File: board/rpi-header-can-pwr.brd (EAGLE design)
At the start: 87 x 56.5 mm, 66 parts, among them J1 U.FL, U1 MCP2515, U2 ADS1015, U3 BME280, U4 RFM69HCW, X2 RASPI_BOARD_B+#_E3

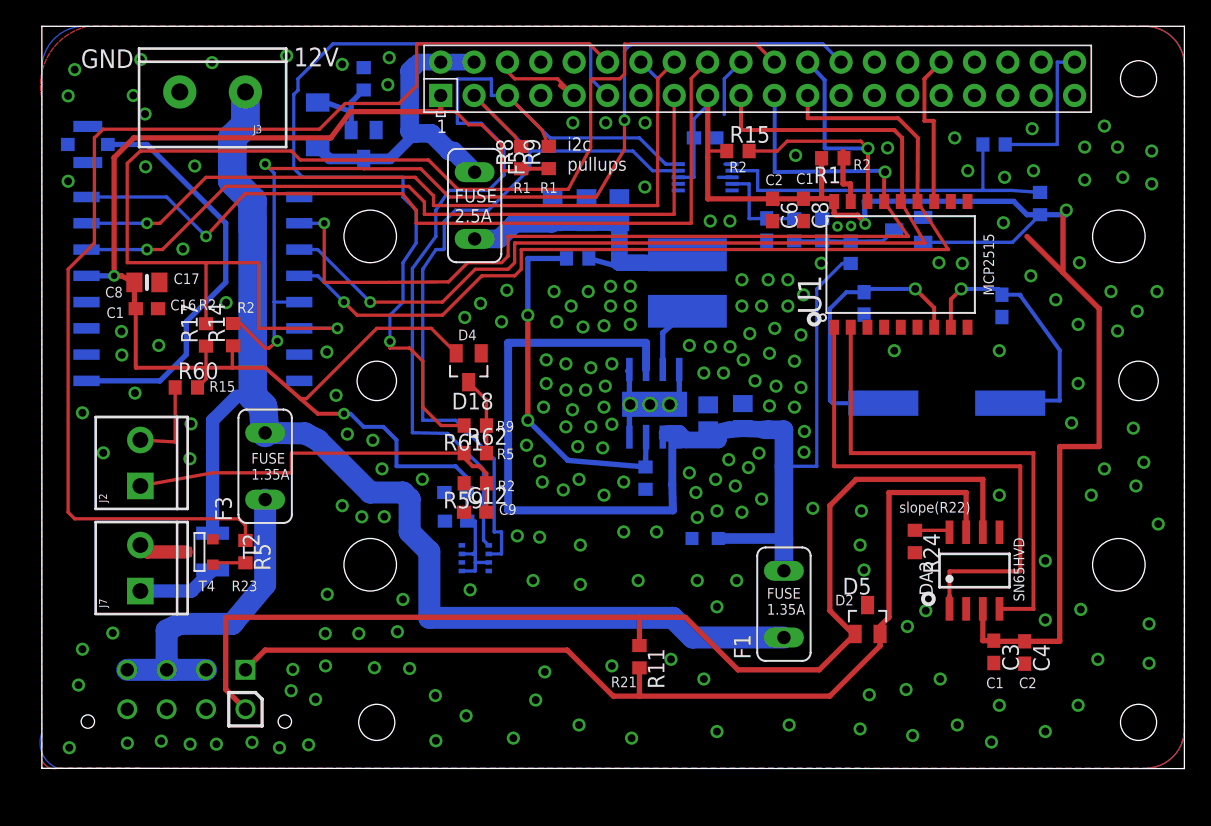
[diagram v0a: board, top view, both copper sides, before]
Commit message: add in219
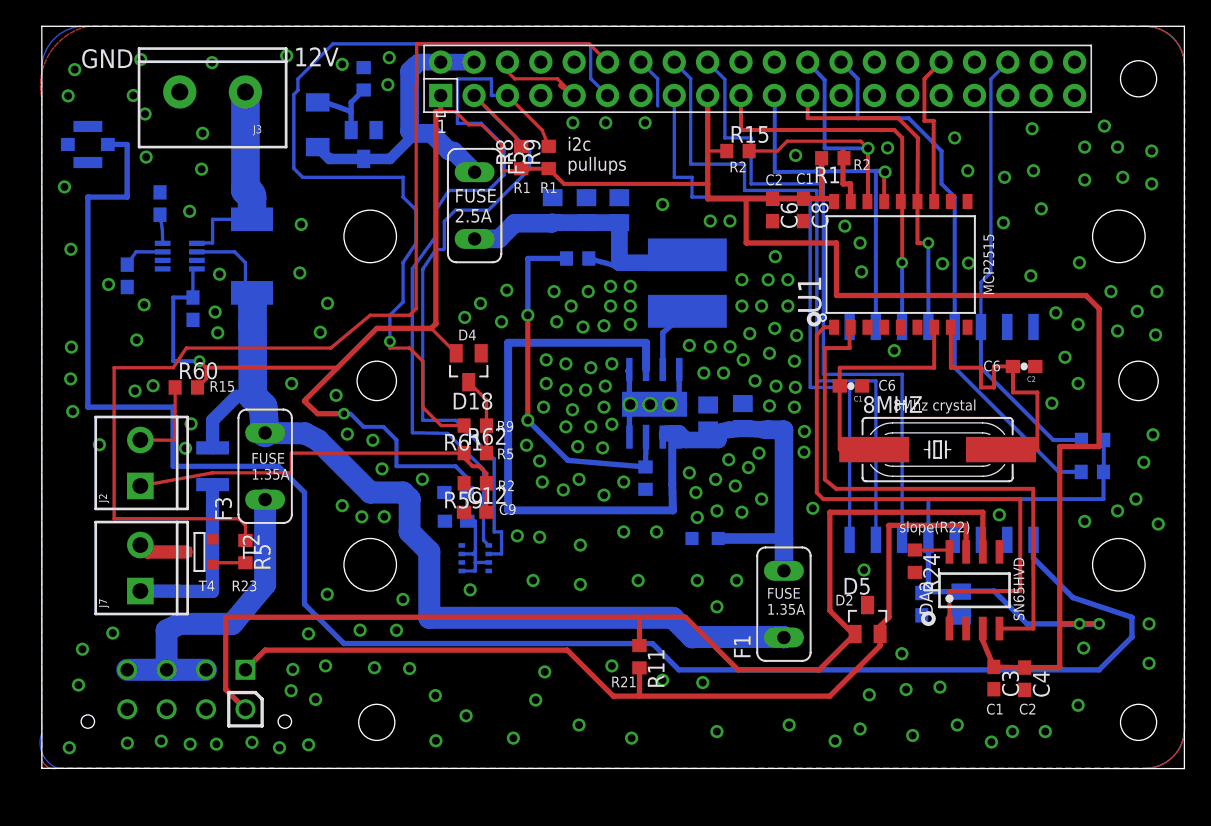
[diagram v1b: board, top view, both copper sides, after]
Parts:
- removed C13: 100n, rcl:C0603
- removed C29: 10nF, eagle-ltspice:C0603
- removed D7: BAS70-04, diode:SOT23
- removed R10: 4.7K, resistor:R0603
- removed R20: 68k, rcl:R0603
- removed R21: 20k, rcl:R0603
- removed R22: 1k, rcl:R0603
- removed R7: 0, resistor:R0603
- removed U2: ADS1015, SparkFun-IC-Conversion:MSOP10
- added C18: 100n, rcl:C0603
- added R12, R13: 10K, microbuilder:0603
- added R19: 0.1/1% (PT2512FK-070R1L), microbuilder:2512
- added U5: INA219BIDCNT, microbuilder:SOT23-8
- moved R17 68.0 mm to (80.0, 25.0), flipped to the bottom, turned to 0 degrees
- moved C17 66.7 mm to (70.0, 12.5), flipped to the bottom, turned to 270 degrees
- moved R14 66.2 mm to (80.0, 22.6), flipped to the bottom, turned to 0 degrees
- moved C16 63.1 mm to (67.0, 12.5), flipped to the bottom, turned to 270 degrees
- moved U4 58.1 mm to (68.5, 25.5), turned to 270 degrees
- moved F4 6.50 mm to (13.0, 23.0)
- moved C1 6.38 mm to (61.6, 29.1), flipped to the top, turned to 180 degrees
- moved C2 4.91 mm to (74.8, 30.6), flipped to the top, turned to 180 degrees
- moved 8MHZ 3.60 mm to (68.2, 24.3), flipped to the top, turned to 0 degrees
- moved C4 2.00 mm to (74.8, 6.82)
- moved C3 2.00 mm to (72.5, 6.87)
- moved DA2 1.50 mm to (71.0, 13.6)
- moved R24 1.50 mm to (66.5, 15.8)
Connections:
- removed net 12V_REFERENCE4: D7.3, R20.2, R21.2, R22.1
- removed net ADC_ALERT: R7.1, X2.40
- removed net ADC_INPUT_1: C29.2, R22.2, U2.4
- removed net N$9: R10.1, R7.2, U2.2
- new net N$15: R13.2, U5.8
- new net N$16: R12.2, U5.7
- new net PRE_SENSE_12V: J3.1, R19.2, U5.1
- new net SCL: U5.5
- new net SDA: U5.6
- net +12V: no longer R20.1
- net +3V3: now also C18.1, U5.4; no longer C13.1, D7.2, R10.2, U2.8
- net GND: now also C18.2, R12.1, R13.1, U5.3; no longer C13.2, C29.1, D7.1, R21.1, U2.1, U2.3
- net I2C_SCL: no longer U2.10
- net I2C_SDA: no longer U2.9
- net LORA_DIO0: now also X2.18; no longer X2.15
- net LORA_DIO2: now also X2.15; no longer X2.18
- net LORA_RST: now also X2.36; no longer X2.22
- net PRE_FUSE_12V: now also R19.1, U5.2; no longer J3.1
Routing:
- net N$5: track 31.1 -> 132.8 mm
- net LORA_RST: track 97.0 -> 34.1 mm, vias 1 -> 0
- net SCK: track 73.5 -> 26.0 mm
- net MOSI: track 75.8 -> 29.6 mm
- net MISO: track 73.1 -> 28.5 mm, vias 2 -> 1
- net LORA_CS: track 75.5 -> 42.0 mm, vias 3 -> 0
- net N$9: track 28.5 -> 0.00 mm
- net +12V: track 95.3 -> 75.9 mm
- net PRE_FUSE_12V: track 90.0 -> 73.8 mm
- net PRE_SENSE_12V: track 0.00 -> 15.9 mm
- net LORA_DIO2: track 63.1 -> 47.2 mm, vias 1 -> 0
- net I2C_SCL: track 71.7 -> 56.5 mm
- net +3V3: track 231.5 -> 246.6 mm
- net I2C_SDA: track 64.2 -> 52.3 mm
- net ADC_ALERT: track 11.6 -> 0.00 mm
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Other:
- board text added: "0.1ohm"
- board text added: "INA219"
- board text added: "can rpi header 2021.03.11 v1.6"
- board text removed: "ADC ALERT"
- board text removed: "ADS1x15"
- board text removed: "R14"
- board text removed: "can rpi header 2021.02.28 v1.6"

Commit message: change back to rj45 (from microfit)
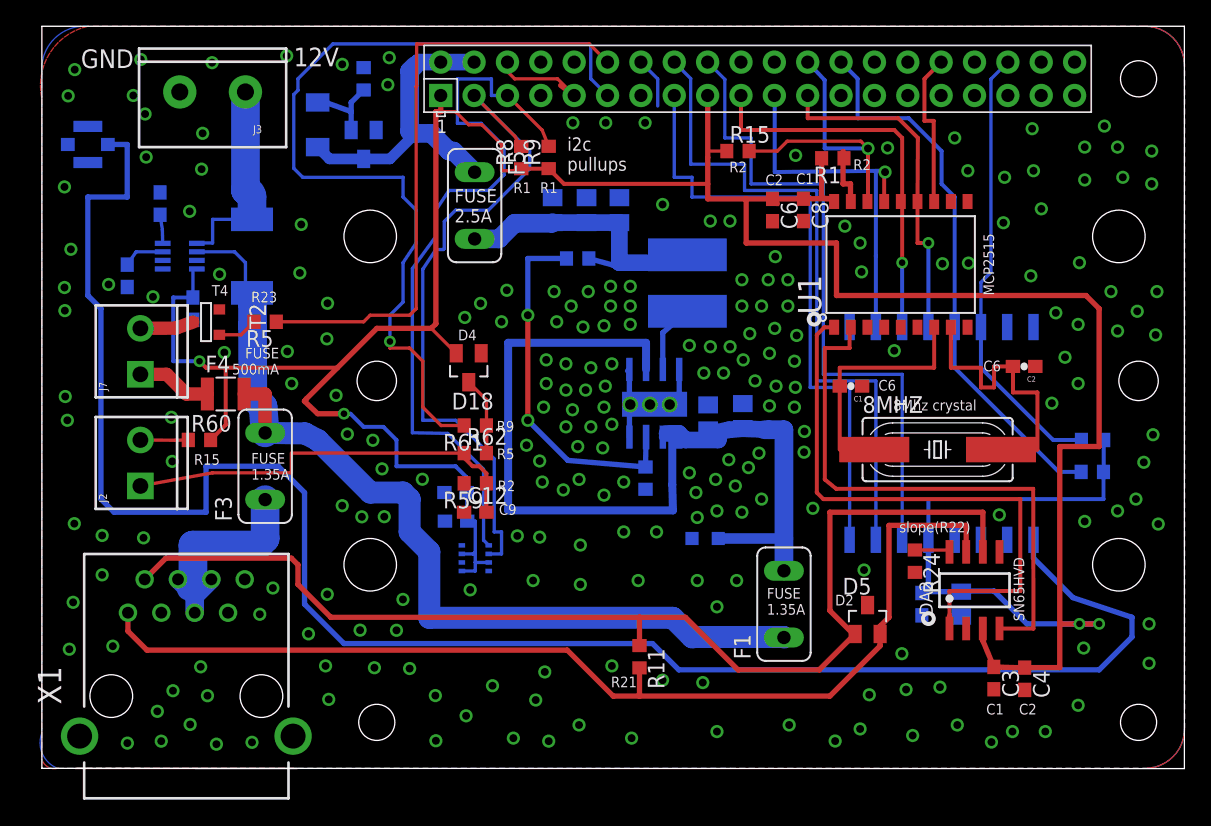
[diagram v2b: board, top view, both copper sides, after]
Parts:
- removed X4: (no value), con-molex-micro-fit-3_0:43045-0812
- added X1: RJ45-8L21-S, con-tycoelectronics:RJ45-SHIELD1
- moved R5 17.6 mm to (17.0, 34.0), turned to 180 degrees
- moved T2 17.5 mm to (12.5, 34.0)
- moved J7 16.5 mm to (7.50, 30.0)
- moved F4 5.59 mm to (14.0, 28.5), flipped to the top, turned to 0 degrees
- moved R60 4.12 mm to (12.0, 25.0)
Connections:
- net CAN_H: now also X1.1; no longer X4.P$1
- net CAN_L: now also X1.2; no longer X4.P$5
- net CAN_PWR: now also X1.4, X1.5, X1.6; no longer X4.P$2, X4.P$3, X4.P$4
- net GND: now also X1.3, X1.7, X1.8, X1.S1, X1.S2; no longer X4.P$6, X4.P$7, X4.P$8
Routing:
- net FAN_PWM: track 83.1 -> 46.3 mm
- net CAN_H: track 71.5 -> 81.8 mm
- net CAN_PWR: track 25.2 -> 17.1 mm
- net N$13: track 13.6 -> 5.72 mm
- net N$5: track 132.8 -> 138.6 mm
- net +3V3: track 246.6 -> 250.8 mm
- net N$10: track 6.67 -> 3.65 mm
- net CAN_L: track 85.3 -> 87.3 mm
- net PRE_FUSE_12V: track 73.8 -> 72.5 mm
- net N$12: track 2.54 -> 3.04 mm
- net GND: vias 231 -> 235

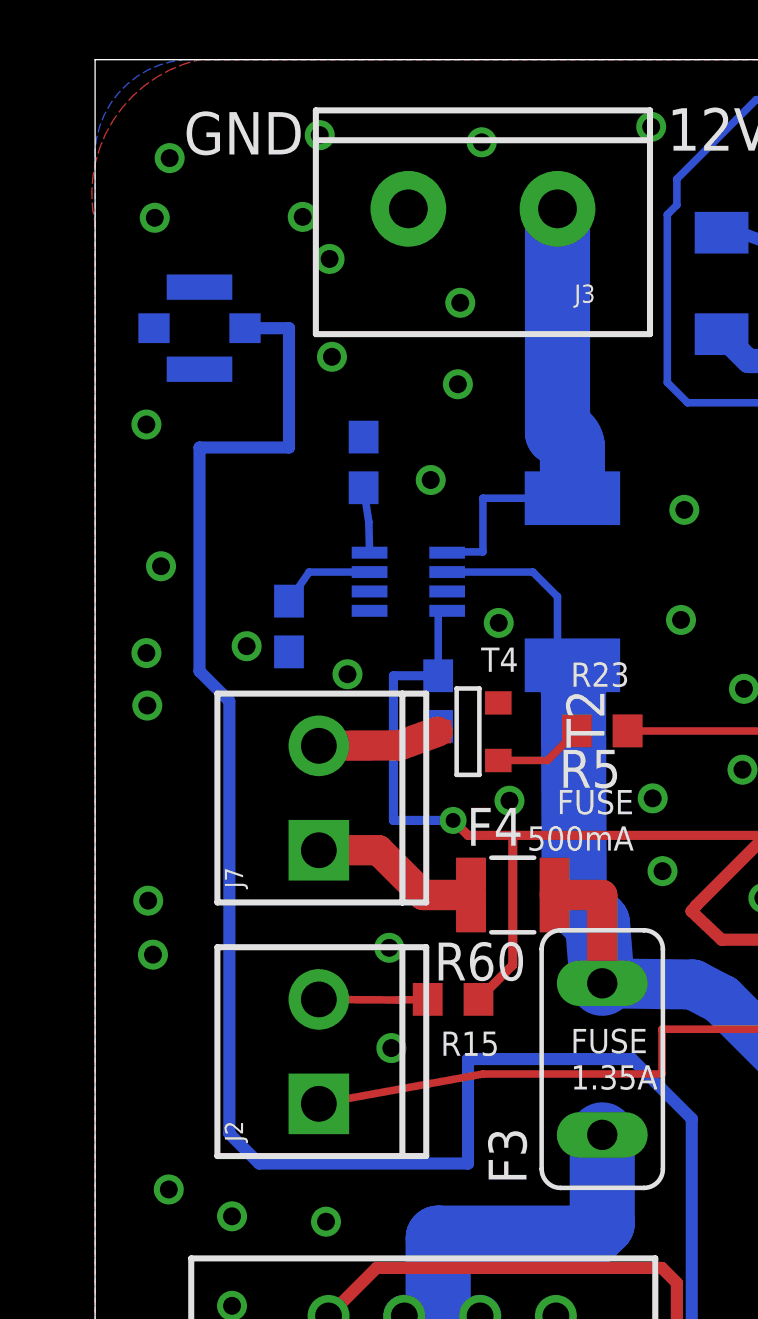
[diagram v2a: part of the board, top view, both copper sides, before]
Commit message: fine tune some labels
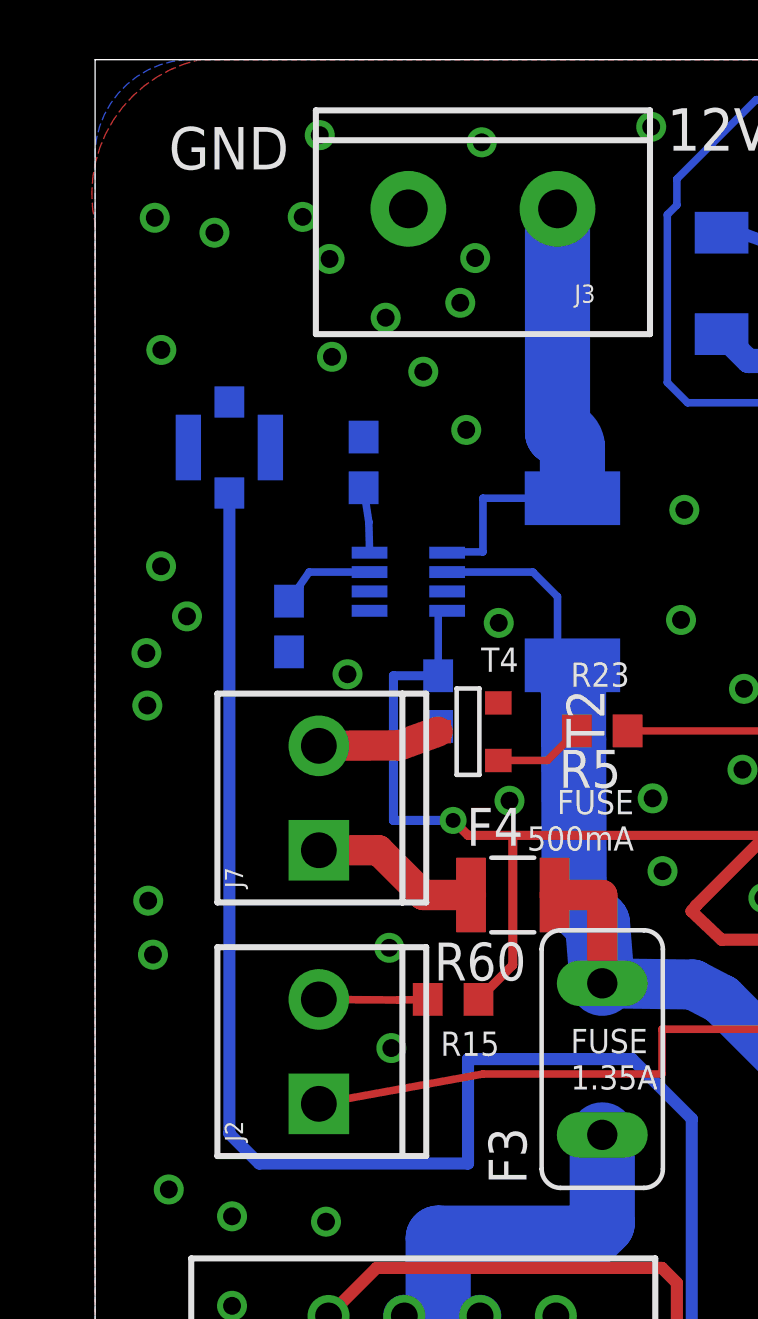
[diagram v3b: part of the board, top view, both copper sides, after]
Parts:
- moved J1 4.12 mm to (4.50, 43.5), turned to 270 degrees
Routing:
- net N$5: track 138.6 -> 128.2 mm
- net GND: vias 235 -> 237
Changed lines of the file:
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@@
 <circle x="58.8" y="34.2" radius="0.412309375" width="0.3048" layer="121"/>
 <text x="60.4" y="12.4" size="0.8128" layer="121">D2</text>
-<text x="15.085" y="46.1866" size="1.524" layer="200" font="vector" rot="R180">can rpi
+<text x="19.085" y="46.1866" size="1.524" layer="200" font="vector" rot="R180">can rpi
 header
 2021.03.11
@@
 2.5A</text>
 <text x="19.17" y="53.45" size="1.4224" layer="121">12V</text>
-<text x="2.97" y="53.32" size="1.4224" layer="121">GND</text>
+<text x="2.47" y="52.82" size="1.4224" layer="121">GND</text>
 <text x="33.1" y="33.4" size="0.8128" layer="121" rot="R180">D4</text>
 <text x="35.98" y="24.35" size="0.8128" layer="121" rot="R180">R5</text>
@@
 <text x="26.2" y="46.6" size="0.8128" layer="122" rot="MR180">T2</text>
 <text x="19.3" y="55.3" size="1.4224" layer="122" rot="MR180">12V</text>
-<text x="6.96" y="53.28" size="1.4224" layer="122" rot="MR0">GND</text>
+<text x="6.46" y="52.78" size="1.4224" layer="122" rot="MR0">GND</text>
 <text x="47.28" y="40.81" size="0.8128" layer="122" rot="MR0">L1</text>
 <text x="52.34" y="45.38" size="0.8128" layer="121">R2</text>
@@
 <circle x="77.86" y="16.7" radius="0.3" width="1.016" layer="122"/>
 <text x="59.9" y="22.2" size="0.8128" layer="122" rot="MR270" align="bottom-right">RFM69HW</text>
-<text x="6.14" y="49.81" size="1.4224" layer="122" distance="12" rot="MR0">lora
+<text x="6.14" y="46.31" size="1.4224" layer="122" distance="12" rot="MR0">lora
 ant</text>
 <text x="71.17" y="28.06" size="0.8128" layer="121" rot="R180">8Mhz crystal</text>
@@
 <element name="U4" library="microbuilder" package="RFMHCW_SMT" value="RFM69HCW" x="68.5" y="25.5" rot="MR270"/>
 <element name="C17" library="microbuilder" package="0805-NO" value="10uF" x="70" y="12.5" rot="MR270"/>
-<element name="J1" library="SparkFun-Connectors" package="U.FL" value="U.FL" x="3.5" y="47.5" rot="MR180">
-<attribute name="SF_ID" value="WRL-09144" x="3.5" y="47.5" size="1.778" layer="28" rot="MR180" display="off"/>
-<attribute name="PROD_ID" value="CONN-09193" x="3.5" y="47.5" size="1.778" layer="28" rot="MR180" display="off"/>
+<element name="J1" library="SparkFun-Connectors" package="U.FL" value="U.FL" x="4.5" y="43.5" rot="MR270">
+<attribute name="SF_ID" value="WRL-09144" x="4.5" y="43.5" size="1.778" layer="28" rot="MR270" display="off"/>
+<attribute name="PROD_ID" value="CONN-09193" x="4.5" y="43.5" size="1.778" layer="28" rot="MR270" display="off"/>
 </element>
 <element name="R14" library="rcl" package="R0603" value="10k" x="79.98" y="22.57" rot="MR0"/>
@@
 <via x="29.96" y="5.54" extent="1-16" drill="0.6"/>
 <via x="21.7" y="32.7" extent="1-16" drill="0.6"/>
-<via x="1.72" y="44.27" extent="1-16" drill="0.6"/>
+<via x="2.22" y="46.77" extent="1-16" drill="0.6"/>
 <via x="80.9" y="48.9" extent="1-16" drill="0.6"/>
 <via x="9.93" y="23.37" extent="1-16" drill="0.6"/>
@@
 <via x="25.2" y="24.98" extent="1-16" drill="0.6"/>
 <via x="7.94" y="46.54" extent="1-16" drill="0.6"/>
-<via x="12.16" y="45.62" extent="1-16" drill="0.6"/>
+<via x="11" y="46.04" extent="1-16" drill="0.6"/>
 <via x="7.86" y="49.82" extent="1-16" drill="0.6"/>
 <via x="12.24" y="48.35" extent="1-16" drill="0.6"/>
@@
 <via x="23.26" y="25.45" extent="1-16" drill="0.6"/>
 <via x="41" y="14" extent="1-16" drill="0.6"/>
-<via x="2.5" y="53.2" extent="1-16" drill="0.6"/>
+<via x="4" y="50.7" extent="1-16" drill="0.6"/>
 <contactref element="U3" pad="1"/>
 <contactref element="U3" pad="7"/>
@@
 <contactref element="R12" pad="1"/>
 <contactref element="C18" pad="2"/>
-<via x="5.08" y="36.84" extent="1-16" drill="0.6"/>
+<via x="3.08" y="37.84" extent="1-16" drill="0.6"/>
 <via x="2.21" y="39.52" extent="1-16" drill="0.6"/>
 <via x="1.75" y="34.85" extent="1-16" drill="0.6"/>
 <via x="13.89" y="31.66" extent="1-16" drill="0.6"/>
 <via x="13.53" y="37.62" extent="1-16" drill="0.6"/>
-<via x="11.25" y="42.41" extent="1-16" drill="0.6"/>
+<via x="12.44" y="44.09" extent="1-16" drill="0.6"/>
 <via x="19.64" y="37.72" extent="1-16" drill="0.6"/>
 <via x="19.75" y="41.41" extent="1-16" drill="0.6"/>
@@
 <via x="17.59" y="13.73" extent="1-16" drill="0.6"/>
 <via x="12.09" y="7.73" extent="1-16" drill="0.6"/>
+<via x="9.74" y="47.85" extent="1-16" drill="0.6"/>
+<via x="12.74" y="49.85" extent="1-16" drill="0.6"/>
 </signal>
 <signal name="CAN_TX">
@@
 <contactref element="U4" pad="1P"/>
 <contactref element="J1" pad="P$3"/>
-<wire x1="5.025" y1="47.5" x2="6.5" y2="47.5" width="0.4064" layer="16"/>
-<wire x1="6.5" y1="47.5" x2="6.5" y2="43.5" width="0.4064" layer="16"/>
 <wire x1="18" y1="23" x2="20" y2="21" width="0.4064" layer="16"/>
 <wire x1="20" y1="21" x2="20" y2="12.5" width="0.4064" layer="16"/>
@@
 <wire x1="78.5" y1="13" x2="75.5" y2="16" width="0.4064" layer="16"/>
 <wire x1="75.5" y1="16" x2="75.5" y2="17.4" width="0.4064" layer="16"/>
-<wire x1="6.5" y1="43.5" x2="3.5" y2="43.5" width="0.4064" layer="16"/>
-<wire x1="3.5" y1="43.5" x2="3.5" y2="36" width="0.4064" layer="16"/>
 <wire x1="18" y1="23" x2="12.5" y2="23" width="0.4064" layer="16"/>
 <wire x1="12.5" y1="23" x2="12.5" y2="19.5" width="0.4064" layer="16"/>
 <wire x1="12.5" y1="19.5" x2="5.5" y2="19.5" width="0.4064" layer="16"/>
 <wire x1="5.5" y1="19.5" x2="4.5" y2="20.5" width="0.4064" layer="16"/>
-<wire x1="4.5" y1="20.5" x2="4.5" y2="35" width="0.4064" layer="16"/>
-<wire x1="4.5" y1="35" x2="3.5" y2="36" width="0.4064" layer="16"/>
+<wire x1="4.5" y1="20.5" x2="4.5" y2="41.975" width="0.4064" layer="16"/>
 </signal>
 <signal name="LORA_CS">
